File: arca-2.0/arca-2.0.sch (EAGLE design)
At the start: 204 parts, among them IC1 MCP6N11R, IC2 MCP6N11R, IC3 MCP6N11R, IC4 MCP6N11R, IC5 LM324D, IC6 LM324D, SW1 1101M2S3CQE2, SW2 1101M2S3CQE2, T1 FQP30N06L, T2 FQP30N06L, T3 FQP30N06L, T4 FQP30N06L, T5 FQP30N06L, T6 FQP30N06L, X1 2540-5

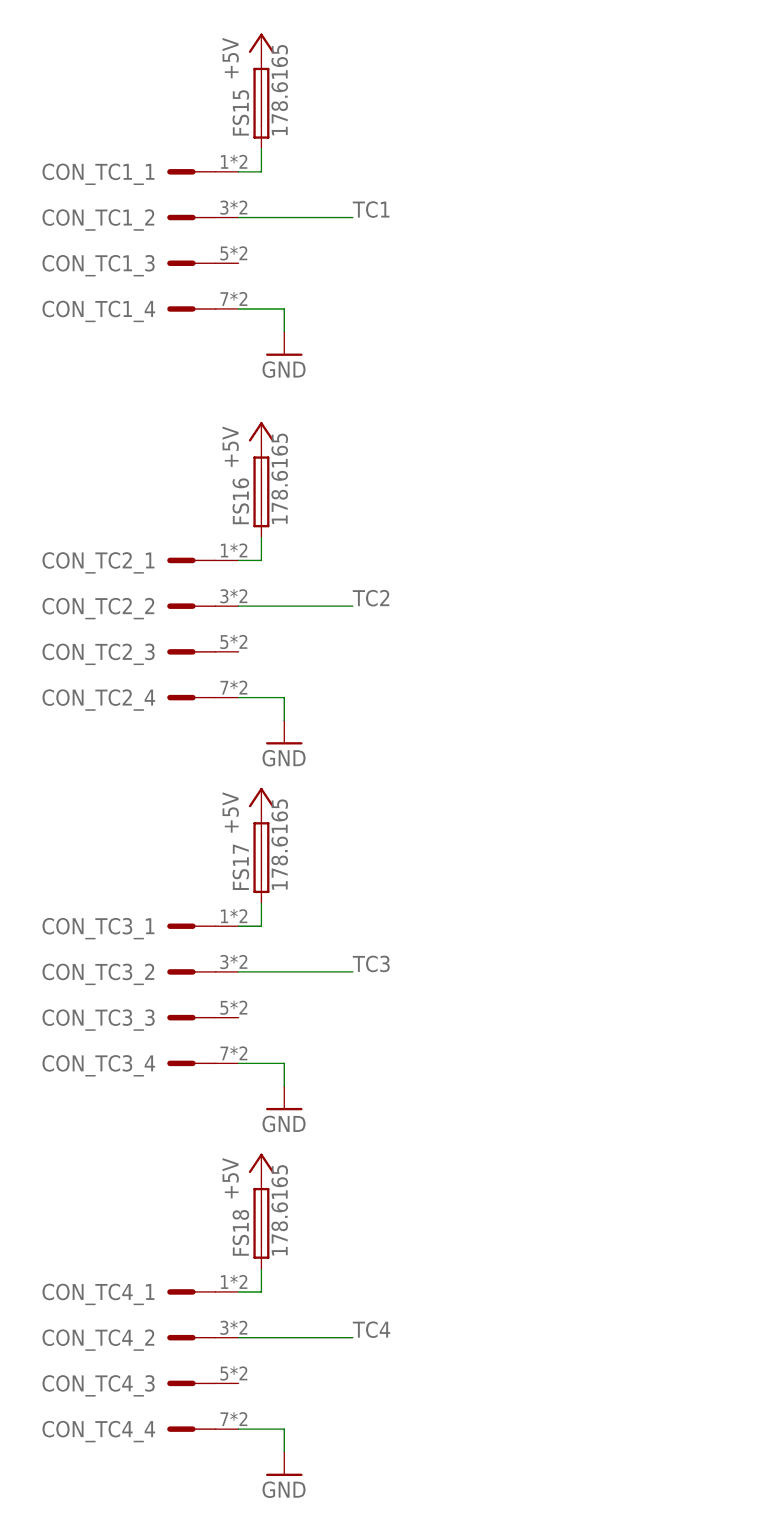
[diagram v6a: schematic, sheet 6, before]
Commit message: found issues with connector orientation
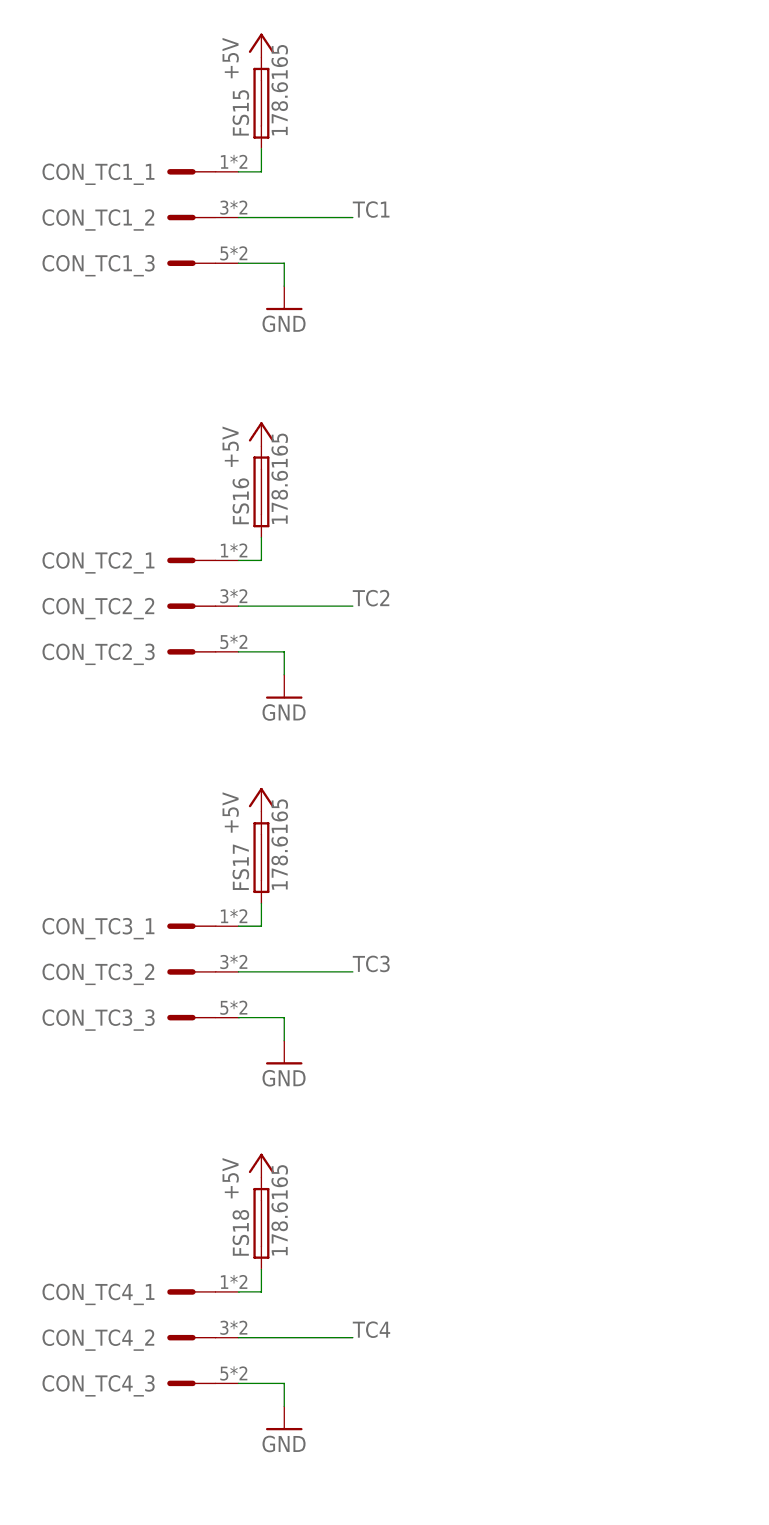
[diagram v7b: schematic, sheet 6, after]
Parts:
- CON_TC1, CON_TC2, CON_TC3, CON_TC4: value LPTA-4POS -> LPTA-3POS; device con-phoenix-5mm:LPTA-4POS -> con-phoenix-5mm:LPTA-3POS
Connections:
- net GND: now also CON_TC1_3.SK, CON_TC2_3.SK, CON_TC3_3.SK, CON_TC4_3.SK; no longer CON_TC1_4.SK, CON_TC2_4.SK, CON_TC3_4.SK, CON_TC4_4.SK
